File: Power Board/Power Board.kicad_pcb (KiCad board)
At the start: 2 copper layers, 80 x 45.7 mm, 172 parts, among them J1 Conn_02x15_Counter_Clockwise, Q1 SI7135DP, Q2 SI7135DP, Q3 SI7135DP, Q4 SI7135DP, Q5 SI7135DP, Q6 SI7135DP, U1 LTC4417CGN, U2 TPS54308DDC, U3 TPS54308DDC, U4 LTC3130-1

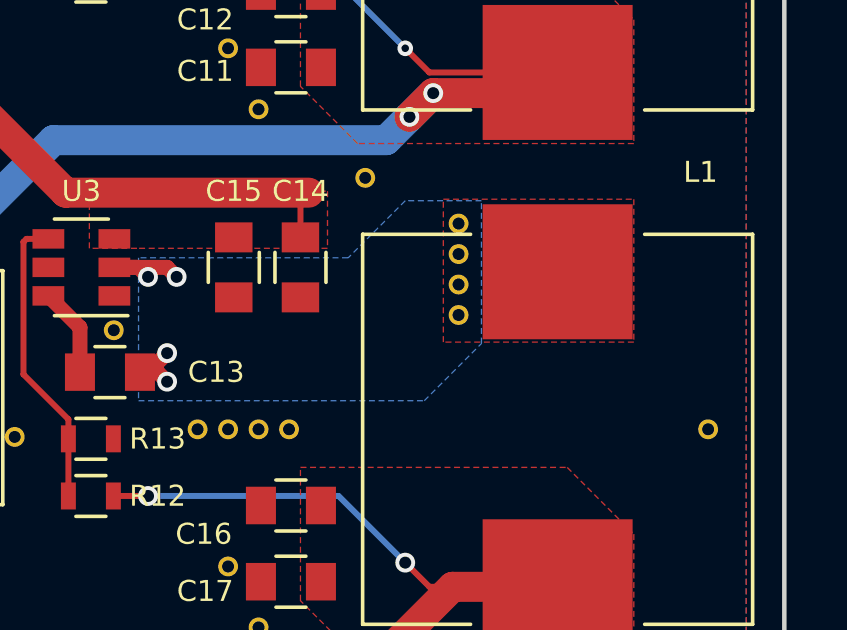
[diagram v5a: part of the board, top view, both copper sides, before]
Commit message: Made the edge connector GND connections wider
Also a few minor cosmetic changes
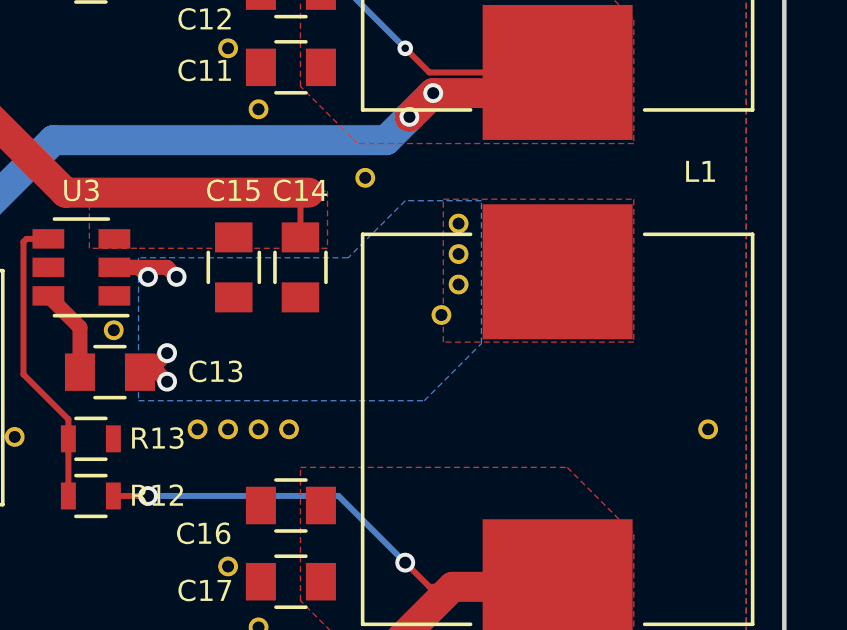
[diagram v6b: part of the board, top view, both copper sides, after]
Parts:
- moved REF** 0.57 mm to (121.9, 116.1)
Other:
- board text added: "Power Board v0.4 UAH SHC Spaceport America Cup 2018 Designed by Thomas Bennett"
- board text removed: "Power Board v0.3 UAH SHC Spaceport America Cup 2018 Designed by Thomas Bennett"
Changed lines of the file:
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@@
     (mod_text_size 0.7 0.7)
     (mod_text_width 0.1)
-    (pad_size 2.5 2.3)
+    (pad_size 1.905 7.62)
     (pad_drill 0)
     (pad_to_mask_clearance 0.0254)
@@
   )
   (module "Custom Footprints:VIA_0.66mm" (layer F.Cu)
-    (at 122.4915 116.078)
+    (at 121.92 116.078)
     (fp_text reference REF** (at 0 1.27) (layer F.SilkS) hide
       (effects (font (size 1 1) (thickness 0.15)))
@@
     (fp_line (start -13.97 -1.27) (end -12.7 0) (layer F.Fab) (width 0.15))
     (pad 1 connect rect (at -11.43 -3.81) (size 1.905 7.62) (layers F.Cu F.Mask)
-      (net 3 GND))
+      (net 3 GND) (thermal_width 1.5))
     (pad 2 connect rect (at -8.89 -3.81) (size 1.905 7.62) (layers F.Cu F.Mask)
-      (net 3 GND))
+      (net 3 GND) (thermal_width 1.5))
     (pad 3 connect rect (at -6.35 -3.81) (size 1.905 7.62) (layers F.Cu F.Mask)
       (net 8 /BAT_VCC) (thermal_gap 0.26))
@@
       (net 1 +14V))
     (pad 29 connect rect (at -8.89 -3.81) (size 1.905 7.62) (layers B.Cu B.Mask)
-      (net 3 GND))
+      (net 3 GND) (thermal_width 1.5))
     (pad 30 connect rect (at -11.43 -3.81) (size 1.905 7.62) (layers B.Cu B.Mask)
-      (net 3 GND))
+      (net 3 GND) (thermal_width 1.5))
     (pad 14 connect rect (at 21.59 -3.81) (size 1.905 7.62) (layers F.Cu F.Mask)
-      (net 3 GND))
+      (net 3 GND) (thermal_width 1.5))
     (pad 11 connect rect (at 13.97 -3.81) (size 1.905 7.62) (layers F.Cu F.Mask)
-      (net 3 GND))
+      (net 3 GND) (thermal_width 1.5))
     (pad 12 connect rect (at 16.51 -3.81) (size 1.905 7.62) (layers F.Cu F.Mask)
-      (net 3 GND))
+      (net 3 GND) (thermal_width 1.5))
     (pad 13 connect rect (at 19.05 -3.81) (size 1.905 7.62) (layers F.Cu F.Mask)
       (net 2 +3V3))
@@
       (net 14 /XBEE_VCC))
     (pad 19 connect rect (at 16.51 -3.81) (size 1.905 7.62) (layers B.Cu B.Mask)
-      (net 3 GND))
+      (net 3 GND) (thermal_width 1.5))
     (pad 16 connect rect (at 24.13 -3.81) (size 1.905 7.62) (layers B.Cu B.Mask)
-      (net 3 GND))
+      (net 3 GND) (thermal_width 1.5))
     (pad 17 connect rect (at 21.59 -3.81) (size 1.905 7.62) (layers B.Cu B.Mask)
-      (net 17 +12V))
+      (net 17 +12V) (thermal_width 1.5))
     (pad 18 connect rect (at 19.05 -3.81) (size 1.905 7.62) (layers B.Cu B.Mask)
-      (net 3 GND))
+      (net 3 GND) (thermal_width 1.5))
     (pad 20 connect rect (at 13.97 -3.81) (size 1.905 7.62) (layers B.Cu B.Mask)
-      (net 3 GND))
+      (net 3 GND) (thermal_width 1.5))
   )
   (module "Custom Footprints:CP_Radial_Horiz_D8.0mm_L13.00mm_P3.50mm" (layer F.Cu)
@@
       (xy -8.090303 16.445066) (xy -8.088882 16.519828) (xy -8.076705 16.532544) (xy -8.033329 16.499711)) (layer B.SilkS) (width 0.01))
   )
-  (gr_text "Power Board v0.3\nUAH SHC Spaceport America Cup 2018\nDesigned by Thomas Bennett" (at 95.25 97.155) (layer B.SilkS)
-    (effects (font (size 1 1) (thickness 0.14)) (justify left mirror))
+  (gr_text "Power Board v0.4\nUAH SHC Spaceport America Cup 2018\nDesigned by Thomas Bennett" (at 102.235 97.155) (layer B.SilkS)
+    (effects (font (size 1 1) (thickness 0.15)) (justify left mirror))
   )
   (gr_text 2 (at 55.88 95.25) (layer B.Cu)

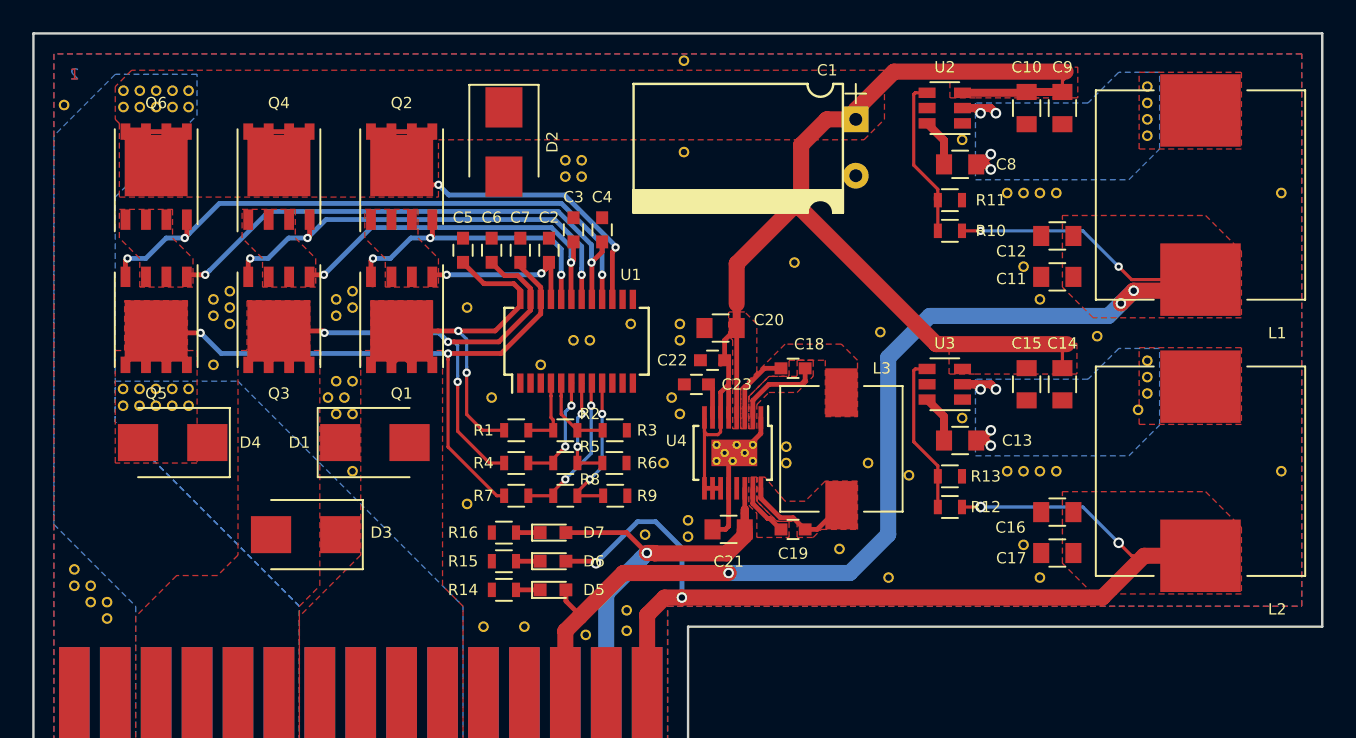
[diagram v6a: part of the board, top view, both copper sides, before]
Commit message: Updated power board to kicad 5
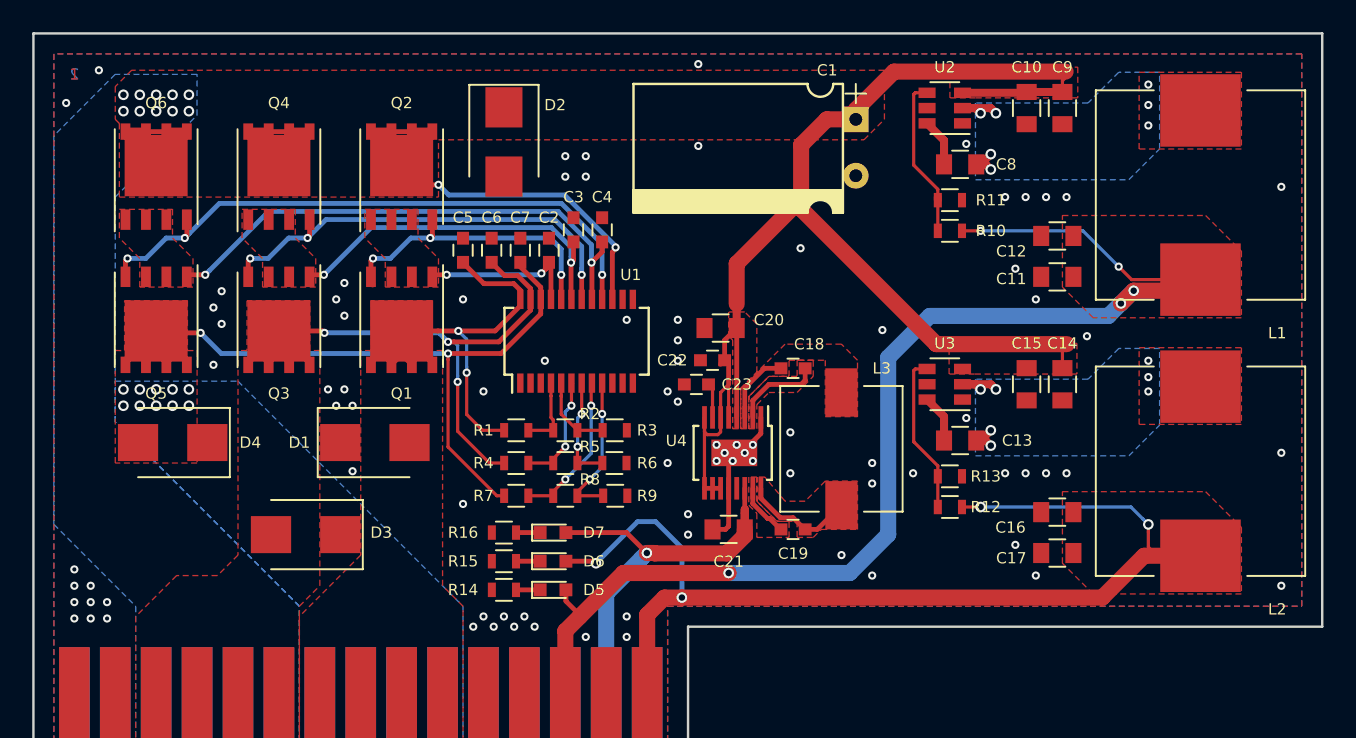
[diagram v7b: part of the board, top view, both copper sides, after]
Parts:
- removed REF** (x103): VIA_0.66mm, Custom Footprints:VIA_0.66mm
- removed REF** (x8): VIA_0.52mm, Custom Footprints:VIA_0.52mm
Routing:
- net /XBEE_VCC: track 70.1 -> 70.9 mm
- net Net-(C8-Pad2): vias 4 -> 7
- net Net-(C13-Pad2): vias 4 -> 7
- net GND: vias 0 -> 87
- net /BAT_BAK_VCC: vias 2 -> 12
- net +14V: vias 2 -> 12
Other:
- net class Default: via_dia 0.66 -> 0.508; via_drill 0.4 -> 0.254
- net class Small: via_dia 0.52 -> 0.508
- board text added: "Power Board v0.5 UAH SHC Spaceport America Cup 2018 Designed by Thomas Bennett"
- board text removed: "Power Board v0.4 UAH SHC Spaceport America Cup 2018 Designed by Thomas Bennett"

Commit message: Forgot an openlog on the control board
Had to get rid of the fault detect pins on the TCs, will have to poll for faults over SPI now
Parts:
- R1: value 90.9 kΩ -> 82.5 kΩ
- R2: value 4.99 kΩ -> 5.49 kΩ
- R3: value 4.99 kΩ -> 11 kΩ
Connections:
- net +14V renamed /VCC_IN
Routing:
- added copper zone on F.Cu, net +14V
